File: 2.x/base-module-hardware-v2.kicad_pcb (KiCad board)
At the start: 4 copper layers, 99.7 x 99.7 mm, 275 parts, among them K1 CONN_3, P1 PINBALL-CONNECTOR, P2 PINBALL-CONNECTOR, P3 SOLENOID-CONNECTOR, P4 CONN_16, P5 CONN_16, P6 HE10-32, Q1 BC846, Q10 DMN6040SSD, Q11 BC846, Q12 BC846, Q13 DMP2240UDM, Q14 DMP2240UDM, Q15 BC846, Q16 BC846, Q17 BC846, Q18 BC846, Q19 DMN6040SSD, Q2 BC846, Q20 DMN6040SSD, Q21 BC846, Q22 BC846, Q23 BC846, Q24 BC846, Q25 BC846, Q26 BC846, Q27 BC846, Q28 BC846, Q29 BSS138, Q3 DMN6040SSD, Q30 FDD5614P, Q31 BC846, Q32 BSS138, Q4 DMN6040SSD, Q5 BC846, Q6 BC846, Q7 BC846, Q8 BC846, Q9 DMN6040SSD, U1 74LVC14, U2 STM32F072R, U3 MCP2562, U4 MC78L05ACH, U5 AP1117IE33G, U6 ZXCT1086E5TA, U7 ZXCT1107SA-7, U8 LM7805CT, U9 MMA8653FC, X1 8.000 MHz

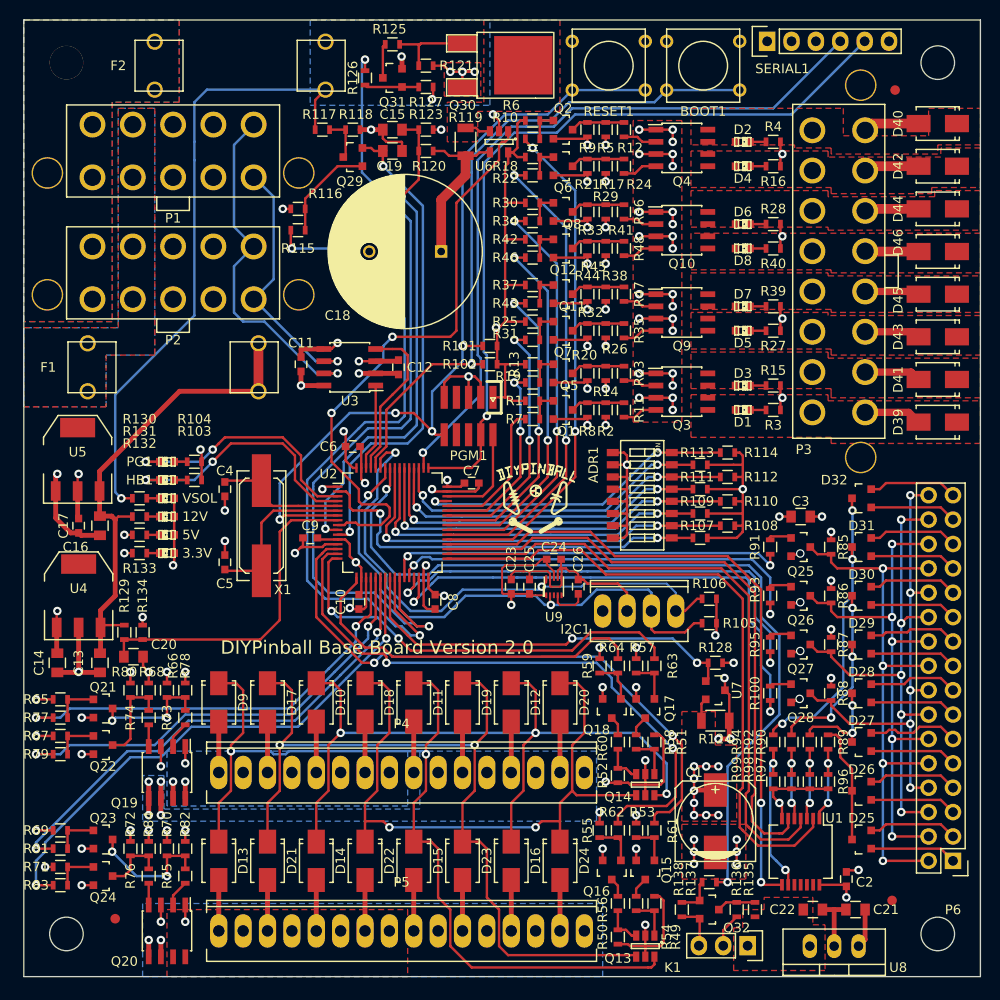
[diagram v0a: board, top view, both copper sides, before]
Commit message: Updated solenoid driver with new resistor arrangement, and changed footprint on switch matrix to a connector we can actually get.
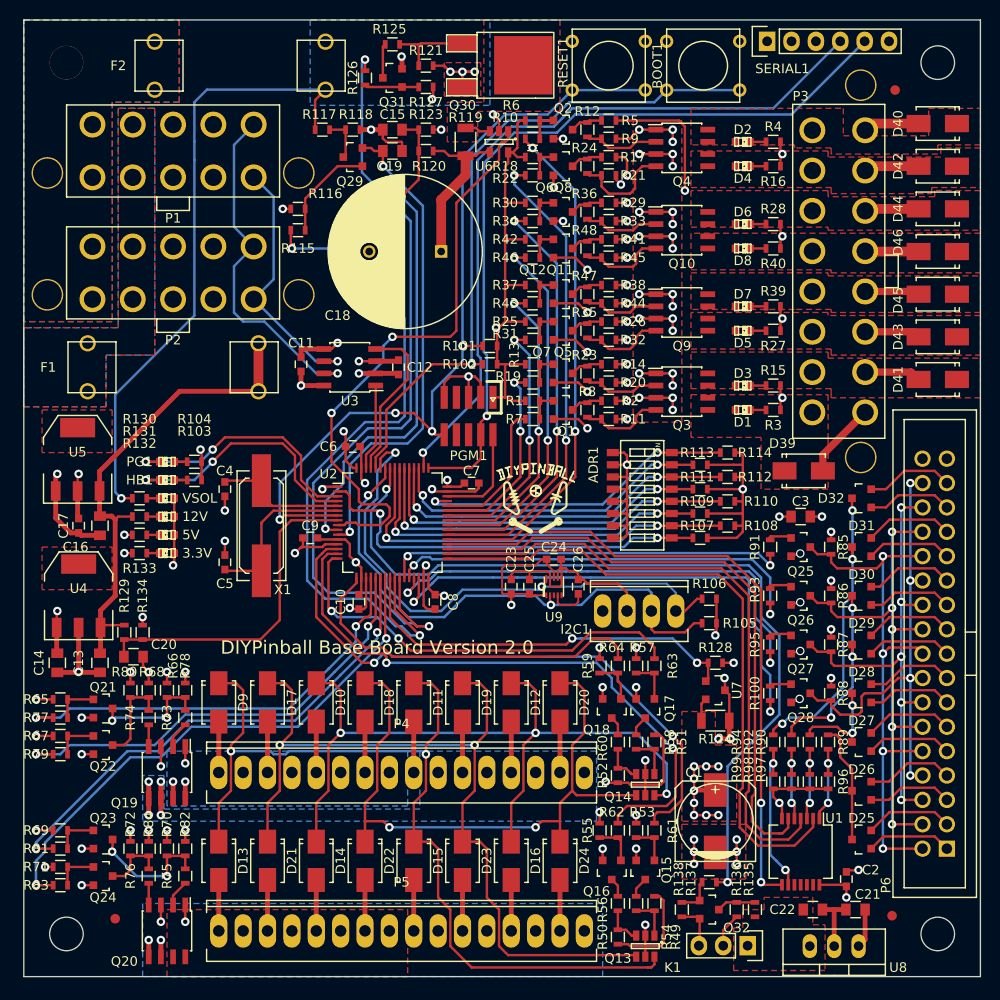
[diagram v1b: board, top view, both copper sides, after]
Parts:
- P6: value HE10-32 -> HE10-34; footprint Pin_Headers:Pin_Header_Straight_2x16 -> PinballParts:BOXHEADER-0.100-34
- moved P6 21.7 mm to (150.8, 146.1), turned to 90 degrees
- moved D39 14.9 mm to (137.2, 127.0), turned to 0 degrees
- moved R11 3.81 mm to (114.6, 120.7)
- moved R12 3.81 mm to (114.6, 91.4)
- moved R23 3.81 mm to (114.6, 116.8)
- moved R24 3.81 mm to (114.6, 95.2)
- moved R35 3.81 mm to (114.6, 112.4)
- moved R36 3.81 mm to (114.6, 100.0)
- moved R47 3.81 mm to (114.6, 108.6)
- moved R48 3.81 mm to (114.6, 103.8)
- moved R20 2.42 mm to (116.8, 117.8), turned to 180 degrees
- moved R21 2.42 mm to (116.8, 96.2), turned to 180 degrees
- moved R32 2.42 mm to (116.8, 113.3), turned to 180 degrees
- moved R33 2.42 mm to (116.8, 101.0), turned to 180 degrees
- moved R44 2.42 mm to (116.8, 109.5), turned to 180 degrees
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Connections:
- R20 pad 1: Net-(Q5-Pad3) -> GND
- R20 pad 2: GND -> Net-(Q3-Pad2)
- R21 pad 1: Net-(Q6-Pad3) -> GND
- R21 pad 2: GND -> Net-(Q4-Pad4)
- R32 pad 1: Net-(Q7-Pad3) -> GND
- R32 pad 2: GND -> Net-(Q9-Pad4)
- R33 pad 1: Net-(Q8-Pad3) -> GND
- R33 pad 2: GND -> Net-(Q10-Pad2)
- R44 pad 1: Net-(Q11-Pad3) -> GND
- R44 pad 2: GND -> Net-(Q9-Pad2)
- R45 pad 1: Net-(Q12-Pad3) -> GND
- R45 pad 2: GND -> Net-(Q10-Pad4)
- R8 pad 1: Net-(Q1-Pad3) -> GND
- R8 pad 2: GND -> Net-(Q3-Pad4)
- R9 pad 1: Net-(Q2-Pad3) -> GND
- R9 pad 2: GND -> Net-(Q4-Pad2)
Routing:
- net (no net): track 0.11 -> 29.3 mm
- net +12V: track 158.9 -> 131.4 mm
- net Net-(Q4-Pad4): track 3.64 -> 10.8 mm
- net Net-(Q10-Pad4): track 3.64 -> 9.09 mm
- net Net-(Q9-Pad4): track 3.64 -> 8.90 mm
- net Net-(Q3-Pad4): track 3.64 -> 8.90 mm
- net Net-(Q10-Pad2): track 3.55 -> 8.40 mm
- net Net-(Q4-Pad2): track 3.55 -> 8.12 mm
- net Net-(Q3-Pad2): track 3.55 -> 8.00 mm
- net Net-(Q9-Pad2): track 3.55 -> 8.00 mm
- net /Switch Matrix/COL2_SWITCHED: track 53.3 -> 51.0 mm
- net Net-(Q8-Pad3): track 5.66 -> 3.41 mm
- net Net-(Q7-Pad3): track 5.66 -> 3.41 mm
- net Net-(Q6-Pad3): track 5.66 -> 3.41 mm
- net Net-(Q5-Pad3): track 5.66 -> 3.41 mm
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
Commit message: Finishing layout updates from review with Mike.
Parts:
- added G***: LOGO, PinballPartsLocal:diypinball-logo-large, B.Cu at (104.8, 132.7)
- C15: value 10u -> 10u DNP
- Q29: value BSS138 -> BSS138 DNP
- R115: value 1K -> 1K DNP
- R116: value 10K -> 10K DNP
- R117: value 95.3K 1% -> 95.3K 1% DNP
- R118: value 5.1K 1% -> 5.1K 1% DNP
- U4: value MC78L05ACH -> MC78L05
- moved U5 0.12 mm to (61.6, 125.7)
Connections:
- ADR1 pad 1: +3.3V -> VCC
- ADR1 pad 2: +3.3V -> VCC
- ADR1 pad 3: +3.3V -> VCC
- ADR1 pad 4: +3.3V -> VCC
- ADR1 pad 5: +3.3V -> VCC
- ADR1 pad 6: +3.3V -> VCC
- ADR1 pad 7: +3.3V -> VCC
- ADR1 pad 8: +3.3V -> VCC
- C10 pad 1: +3.3V -> VCC
- C11 pad 1: +3.3V -> VCC
- C17 pad 1: +3.3V -> VCC
- C2 pad 1: +3.3V -> VCC
- C23 pad 1: +3.3V -> VCC
- C24 pad 1: +3.3V -> VCC
- C25 pad 1: +3.3V -> VCC
- C6 pad 1: +3.3V -> VCC
- C7 pad 1: +3.3V -> VCC
- C8 pad 1: +3.3V -> VCC
- C9 pad 1: +3.3V -> VCC
- I2C1 pad 1: +3.3V -> VCC
- PGM1 pad 1: +3.3V -> VCC
- R1 pad 1: +3.3V -> VCC
- R101 pad 1: +3.3V -> VCC
- R102 pad 1: +3.3V -> VCC
- R105 pad 1: +3.3V -> VCC
- R106 pad 1: +3.3V -> VCC
- R13 pad 1: +3.3V -> VCC
- R133 pad 1: +3.3V -> VCC
- R18 pad 1: +3.3V -> VCC
- R25 pad 1: +3.3V -> VCC
- R30 pad 1: +3.3V -> VCC
- R37 pad 1: +3.3V -> VCC
- R42 pad 1: +3.3V -> VCC
- R6 pad 1: +3.3V -> VCC
- R65 pad 1: +3.3V -> VCC
- R67 pad 1: +3.3V -> VCC
- R69 pad 1: +3.3V -> VCC
- R71 pad 1: +3.3V -> VCC
- U1 pad 14: +3.3V -> VCC
- U2 pad 1: +3.3V -> VCC
- U2 pad 13: +3.3V -> VCC
- U2 pad 19: +3.3V -> VCC
- U2 pad 3: /Control Logic/POWER_GOOD -> /Control Logic/HEARTBEAT
- U2 pad 32: +3.3V -> VCC
- U2 pad 4: /Control Logic/HEARTBEAT -> /Control Logic/POWER_GOOD
- U2 pad 48: +3.3V -> VCC
- U2 pad 64: +3.3V -> VCC
- U3 pad 5: +3.3V -> VCC
- U4 pad 4: (no net) -> GND
- U5 pad 2: +3.3V -> VCC
- U5 pad 4: (no net) -> VCC
- U6 pad 5: +3.3V -> VCC
- U9 pad 1: +3.3V -> VCC
- U9 pad 8: +3.3V -> VCC
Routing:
- net VCC: track 0.00 -> 211.3 mm, vias 0 -> 26
- net +3.3V: track 204.1 -> 0.00 mm, vias 18 -> 0
- net GND: track 275.9 -> 292.0 mm, vias 94 -> 102
- net /Control Logic/POWER_GOOD: track 26.6 -> 24.0 mm, vias 2 -> 0
- net +5V: track 66.0 -> 67.9 mm
- net /Control Logic/HEARTBEAT: track 27.0 -> 28.2 mm, vias 2 -> 0
- added copper zone on F.Cu, net VCC
- added copper zone on Power.Cu, net VCC
- removed copper zone on Power.Cu, net +3.3V
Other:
- board text added: "CANH"
- board text added: "CANL"
- board text added: "GND"
- board text added: "N/C"
- board text added: "RXD"
- board text added: "SCL"
- board text added: "SDA"
- board text added: "TXD"
- board text added: "X"
- board text added: "Y"

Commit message: Logo placement adjustment
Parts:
- moved G*** 0.95 mm to (104.8, 133.7)
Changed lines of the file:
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@@
     (links 617)
     (no_connects 0)
-    (area 55.829999 79.959999 155.625001 179.755001)
+    (area 51.788076 78.0551 160.2549 181.79572)
     (thickness 1.6)
     (drawings 37)
@@
   )
   (module PinballPartsLocal:diypinball-logo-large (layer B.Cu)
-    (at 104.775 132.715 90)
+    (at 104.775 133.6675 90)
     (fp_text reference G*** (at 0 0 90) (layer B.SilkS) hide
       (effects (font (thickness 0.3)) (justify mirror))

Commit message: Adding CAM data
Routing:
- net /Lamp Driver/LAMP_12V: vias 16 -> 15
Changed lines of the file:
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@@
     (thickness 1.6)
     (drawings 37)
-    (tracks 2133)
+    (tracks 2132)
     (zones 0)
     (modules 276)
@@
     (visible_elements 7FFFFF7F)
     (pcbplotparams
-      (layerselection 0x00030_80000001)
+      (layerselection 0x010fc_80000007)
       (usegerberextensions false)
       (excludeedgelayer true)
@@
       (plotinvisibletext false)
       (padsonsilk false)
-      (subtractmaskfromsilk false)
+      (subtractmaskfromsilk true)
       (outputformat 1)
       (mirror false)
-      (drillshape 1)
+      (drillshape 0)
       (scaleselection 1)
-      (outputdirectory ""))
+      (outputdirectory cam/))
   )
   (net 0 "")
@@
   (via (at 127 162.8775) (size 0.889) (layers F.Cu B.Cu) (net 9))
   (segment (start 128.27 162.8775) (end 127 162.8775) (width 0.254) (layer F.Cu) (net 9))
-  (via (at 128.27 157.7975) (size 0.889) (layers F.Cu B.Cu) (net 9))
   (segment (start 127 157.7975) (end 125.73 157.7975) (width 0.254) (layer F.Cu) (net 9))
   (via (at 125.73 157.7975) (size 0.889) (layers F.Cu B.Cu) (net 9))
